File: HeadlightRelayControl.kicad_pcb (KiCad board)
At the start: 2 copper layers, 49.5 x 49.5 mm, 30 parts, among them P1 CONN_01X03, P2 CONN_01X02, P3 CONN_01X02, P4 CONN_2, Q1 2N3904, Q2 2N3904

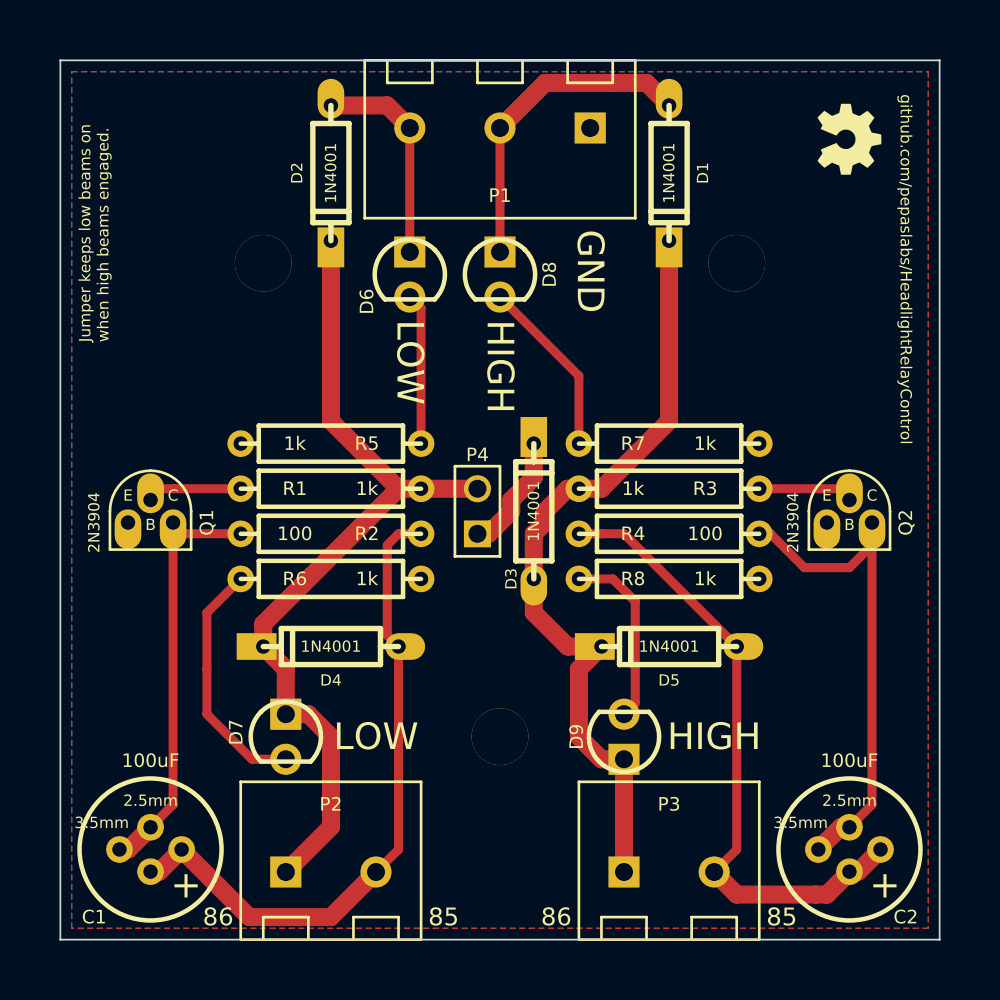
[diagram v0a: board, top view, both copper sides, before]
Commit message: bugfix: a 1/4 watt resistor was seeing 500mW.  broke it up into four 1/4w resistors.  this is release v2.
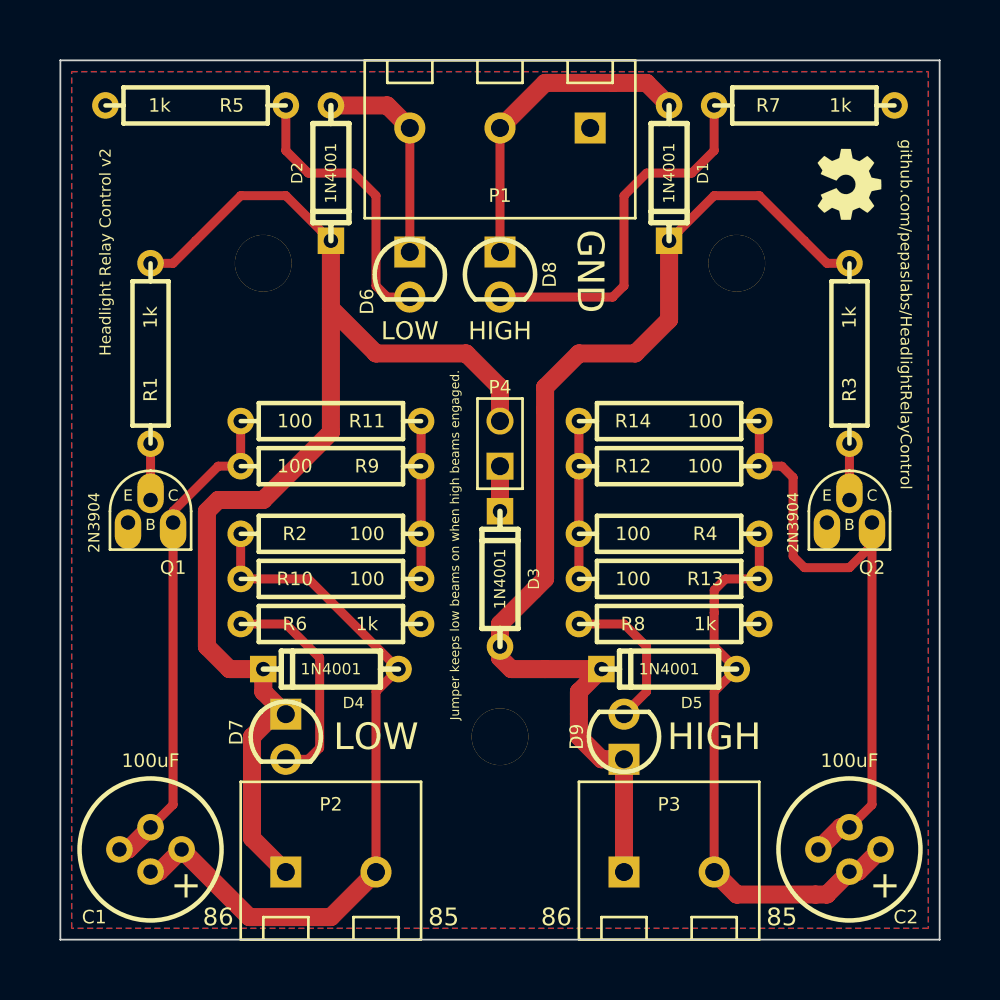
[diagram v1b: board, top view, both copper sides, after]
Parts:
- added R10: 100, R_AXIAL_0W25_059A, F.Cu at (94.0, 95.2)
- added R11: 100, R_AXIAL_0W25_059A, F.Cu at (104.1, 86.4)
- added R12: 100, R_AXIAL_0W25_059A, F.Cu at (113.0, 88.9)
- added R13: 100, R_AXIAL_0W25_059A, F.Cu at (123.2, 95.2)
- added R14: 100, R_AXIAL_0W25_059A, F.Cu at (113.0, 86.4)
- added R9: 100, R_AXIAL_0W25_059A, F.Cu at (104.1, 88.9)
- D1, D2, D3, D4, D5: footprint DIODE_3 -> DIODE_3_059A
- moved R5 20.5 mm to (96.5, 68.6)
- moved R7 20.5 mm to (120.7, 68.6)
- moved R2 10.2 mm to (94.0, 92.7), turned to 0 degrees
- moved R4 10.2 mm to (123.2, 92.7), turned to 180 degrees
- moved R3 5.68 mm to (128.3, 87.6), turned to 90 degrees
- moved R1 5.68 mm to (88.9, 87.6), turned to 90 degrees
- moved D3 4.26 mm to (108.6, 99.1)
- moved P4 4.02 mm to (108.6, 87.6)
- moved G*** 2.54 mm to (128.3, 73.0)
- moved R6 2.54 mm to (94.0, 97.8)
- moved R8 2.54 mm to (113.0, 97.8)
- moved D4 1.27 mm to (102.9, 100.3)
- moved D5 1.27 mm to (121.9, 100.3)
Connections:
- C1 pad 2: N-0000020 -> N-0000022
- C2 pad 2: N-0000010 (its old number) -> N-0000013
- Q1 pad 3: N-0000020 -> N-0000022
- Q2 pad 3: N-0000010 (its old number) -> N-0000013
- R2 pad 2: N-0000020 -> N-0000015
- R4 pad 2: N-0000010 (its old number) -> N-0000014
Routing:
- net N-0000013: track 0.00 -> 35.6 mm
- net N-0000010 (its old number): track 28.9 -> 0.00 mm
- net N-0000022: track 0.00 -> 28.0 mm
- net N-0000020: track 24.0 -> 0.00 mm
- net LowBeamControl: track 48.1 -> 70.9 mm
- net HighBeamControl: track 44.8 -> 61.8 mm
- net N-000004: track 10.1 -> 21.0 mm
- net N-0000015: track 0.00 -> 8.89 mm
- net N-0000014: track 0.00 -> 8.89 mm
- net N-000003: track 8.52 -> 15.9 mm
- net N-0000016: track 6.77 -> 2.54 mm
- net N-0000017: track 37.2 -> 41.3 mm
- net N-0000024: track 35.7 -> 33.2 mm
- net N-0000018: track 5.34 -> 3.18 mm
- net N-0000023: track 5.34 -> 3.18 mm
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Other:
- board text added: "Headlight Relay Control v2"

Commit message: removing extraneous transistors. updated board labelling.
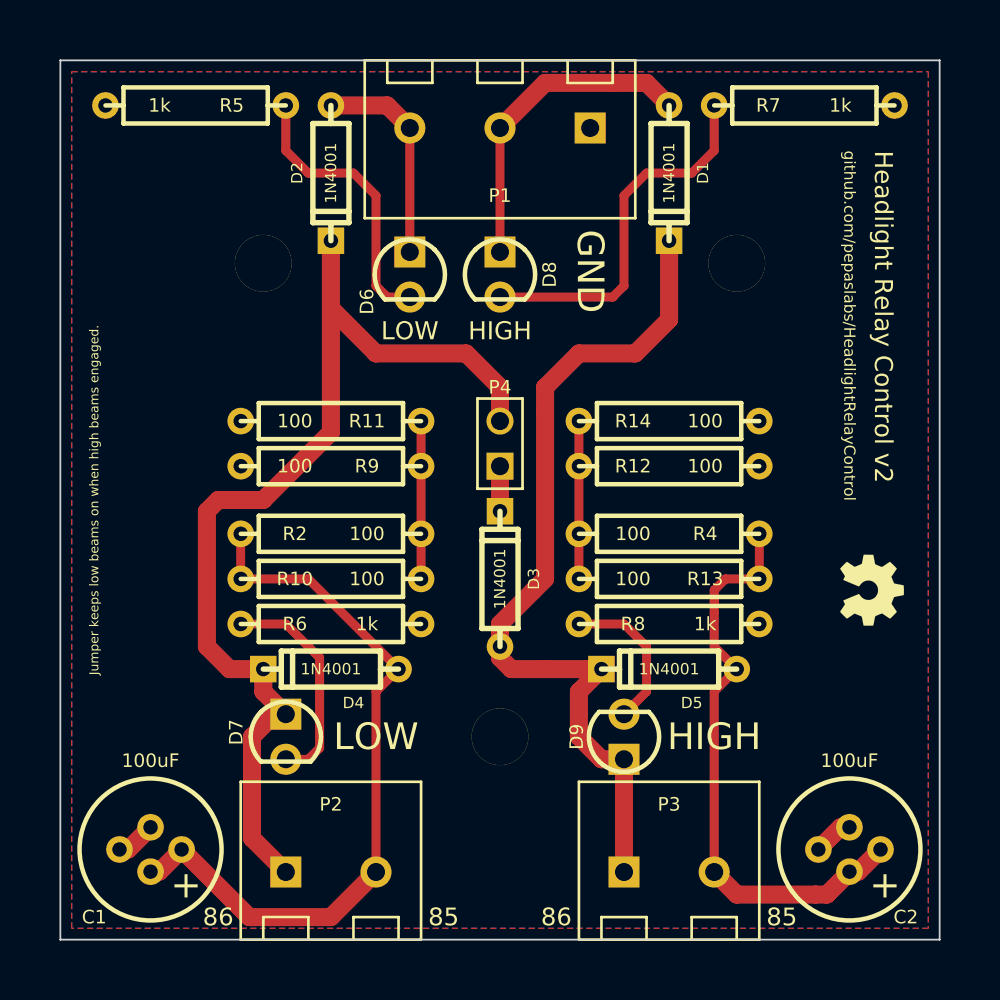
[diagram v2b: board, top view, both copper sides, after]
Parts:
- removed Q1, Q2: 2N3904, TO-92_Q_EBC
- removed R1, R3: 1k, R_AXIAL_0W25_059A
- moved G*** 22.9 mm to (129.5, 95.9)
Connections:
- C1 pad 2: N-0000022 -> GND
- C2 pad 2: N-0000013 (its old number) -> GND
- R11 pad 2: N-0000022 -> GND
- R12 pad 2: N-0000013 (its old number) -> GND
- R14 pad 2: N-0000013 (its old number) -> GND
- R9 pad 2: N-0000022 -> GND
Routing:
- net N-0000013 (its old number): track 35.6 -> 0.00 mm
- net N-0000022: track 28.0 -> 0.00 mm
- net HighBeamControl: track 61.8 -> 49.0 mm
- net LowBeamControl: track 70.9 -> 58.1 mm
- net GND: track 0.00 -> 4.54 mm
- net N-0000023: track 3.18 -> 0.00 mm
- net N-0000018 (its old number): track 3.18 -> 0.00 mm
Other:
- board text added: "+"
- board text added: "-"

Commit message: Added corner mounting holes.
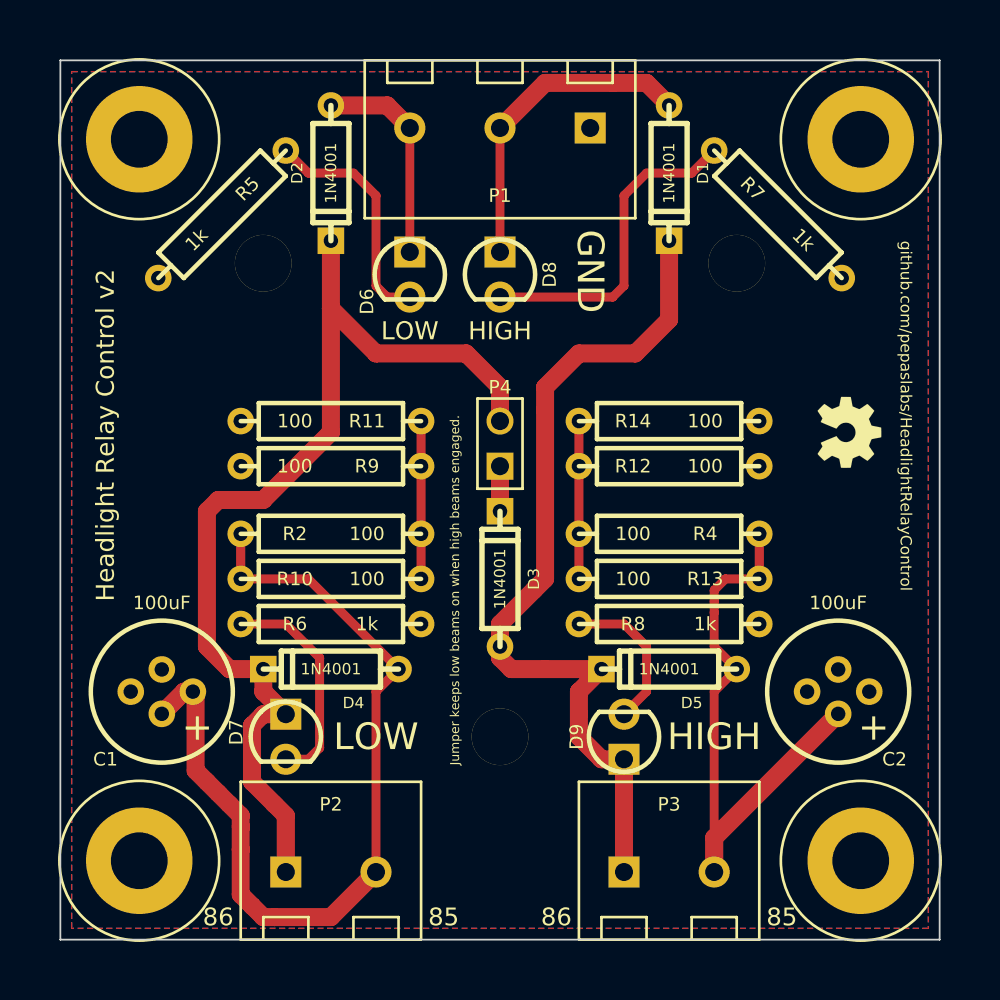
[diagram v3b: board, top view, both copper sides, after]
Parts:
- added H10: HOLE, hole_M3, F.Cu at (88.3, 111.1)
- added H4: HOLE, hole_M3, F.Cu at (88.3, 70.5)
- added H8: HOLE, hole_M3, F.Cu at (128.9, 70.5)
- added H9: HOLE, hole_M3, F.Cu at (128.9, 111.1)
- moved G*** 8.98 mm to (128.3, 87.0)
- moved C1 8.91 mm to (89.5, 101.6)
- moved C2 8.91 mm to (127.6, 101.6)
- moved R5 2.54 mm to (96.5, 71.1), turned to 225 degrees
- moved R7 2.54 mm to (120.7, 71.1), turned to 315 degrees
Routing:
- net N-0000017: track 41.3 -> 49.5 mm
- net GND: track 4.54 -> 0.00 mm
- net N-000009: track 15.9 -> 13.4 mm
- net N-000003: track 21.0 -> 18.5 mm
- net N-0000024: track 33.2 -> 34.1 mm

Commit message: adding v3 board design with constant current sinks on relay coils.
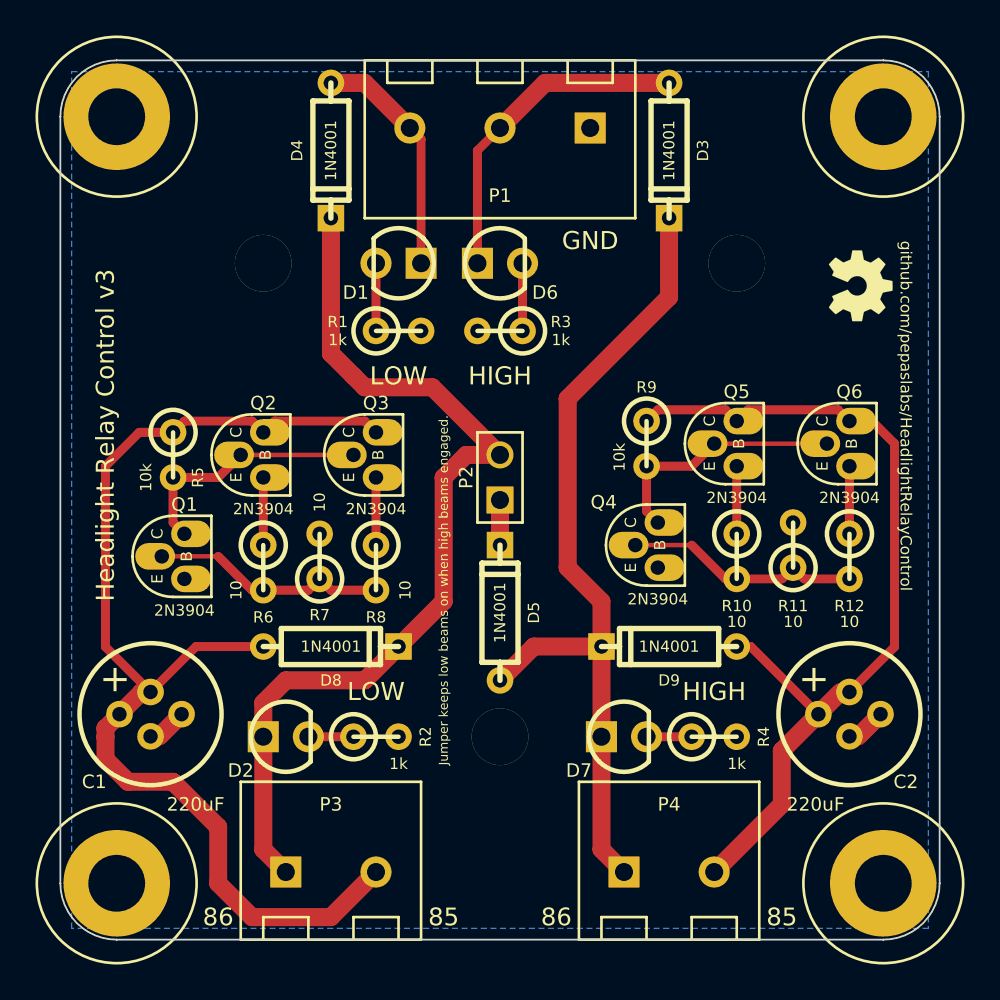
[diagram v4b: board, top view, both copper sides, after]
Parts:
- removed H4: HOLE, hole_M3
- removed R13, R14: 100, R_AXIAL_0W25_059A
- added H7: HOLE, hole_M3, F.Cu at (130.2, 112.4)
- added Q1: 2N3904, TO-92_Q_EBC, F.Cu at (90.8, 95.2)
- added Q2: 2N3904, TO-92_Q_EBC, F.Cu at (95.2, 89.5)
- added Q3: 2N3904, TO-92_Q_EBC, F.Cu at (101.6, 89.5)
- added Q4: 2N3904, TO-92_Q_EBC, F.Cu at (117.5, 94.6)
- added Q5: 2N3904, TO-92_Q_EBC, F.Cu at (121.9, 88.9)
- added Q6: 2N3904, TO-92_Q_EBC, F.Cu at (128.3, 88.9)
- added R1: 1k, R_AXIAL_0W25_V_059A, F.Cu at (101.6, 81.3)
- added R3: 1k, R_AXIAL_0W25_V_059A, F.Cu at (109.9, 81.3)
- C1, C2: value 100uF -> 220uF
- D1, D2: value 1N4001 -> LED; footprint DIODE_3_059A -> LED_3MM_069A
- D8, D9: value LED -> 1N4001; footprint LED_3MM_069A -> DIODE_3_059A
- P2: value CONN_01X02 -> CONN_2; footprint TERMINAL_BLOCK_2_5mm -> PIN_ARRAY_2X1
- P4: value CONN_2 -> CONN_01X02; footprint PIN_ARRAY_2X1 -> TERMINAL_BLOCK_2_5mm
- R10, R11, R12: value 100 -> 10; footprint R_AXIAL_0W25_059A -> R_AXIAL_0W25_V_059A
- R2, R4: value 100 -> 1k; footprint R_AXIAL_0W25_059A -> R_AXIAL_0W25_V_059A
- R5: value 1k -> 10k; footprint R_AXIAL_0W25_059A -> R_AXIAL_0W25_V_059A
- R6, R7, R8: value 1k -> 10; footprint R_AXIAL_0W25_059A -> R_AXIAL_0W25_V_059A
- R9: value 100 -> 10k; footprint R_AXIAL_0W25_059A -> R_AXIAL_0W25_V_059A
- moved H8 59.3 mm to (87.0, 112.4)
- moved H10 41.9 mm to (87.0, 69.2)
- moved H9 41.9 mm to (130.2, 69.2)
- moved D2 35.8 mm to (95.2, 104.1), turned to 0 degrees
- moved D4 33.2 mm to (99.1, 67.3), turned to 270 degrees
- moved D3 33.1 mm to (118.1, 67.3), turned to 270 degrees
- moved R7 32.8 mm to (98.4, 95.2), turned to 90 degrees
- moved R10 28.1 mm to (121.9, 92.7), turned to 270 degrees
- moved H2 26.7 mm to (95.2, 77.5)
- moved H3 26.7 mm to (121.9, 77.5)
- moved P4 25.9 mm to (118.1, 111.8), turned to 0 degrees
- moved D8 25.9 mm to (95.2, 99.1), turned to 0 degrees
- moved P2 24.2 mm to (108.6, 89.5), turned to 90 degrees
- moved R11 22.5 mm to (125.1, 94.6), turned to 90 degrees
- moved P3 19.0 mm to (99.1, 111.8)
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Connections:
- C1 pad 1: N-0000017 -> N-000007
- C2 pad 1: N-0000024 -> N-000002
- D1 pad 1: HighBeamSignal -> LowBeamSignal
- D1 pad 2: HighBeamControl -> N-0000015
- D2 pad 1: LowBeamSignal -> LowBeamControl
- D2 pad 2: LowBeamControl -> N-0000030
- D3 pad 1: HighBeamControl -> HighBeamSignal
- D3 pad 2: N-0000022 -> HighBeamControl
- D4 pad 1: N-0000017 -> LowBeamSignal
- D5 pad 1: N-0000024 -> HighBeamControl
- D5 pad 2: HighBeamControl -> N-0000028
- D6 pad 1: LowBeamSignal -> HighBeamSignal
- D6 pad 2: N-000009 -> N-0000016
- D7 pad 1: LowBeamControl -> HighBeamControl
- D7 pad 2: N-0000023 -> N-0000014
- D8 pad 1: HighBeamSignal -> N-000007
- D8 pad 2: N-000003 -> LowBeamControl
- D9 pad 1: HighBeamControl -> N-000002
- D9 pad 2: N-000008 -> HighBeamControl
- P2 pad 1: LowBeamControl -> N-0000028
- P2 pad 2: N-0000017 -> LowBeamControl
- P3 pad 1: HighBeamControl -> LowBeamControl
- P3 pad 2: N-0000024 -> N-000007
- P4 pad 1: N-0000022 -> HighBeamControl
- P4 pad 2: LowBeamControl -> N-000002
- R10 pad 1: N-0000017 -> N-000005
- R10 pad 2: N-0000011 -> N-000004
- R11 pad 1: N-0000011 -> N-000004
- R12 pad 1: N-0000016 -> N-000006
- R12 pad 2: GND -> N-000004
- R2 pad 1: N-0000017 -> N-0000030
- R2 pad 2: N-0000011 -> GND
- R4 pad 1: N-0000024 -> N-0000014
- R4 pad 2: N-0000016 -> GND
- R5 pad 1: N-000009 -> N-000007
- R5 pad 2: GND -> N-000001
- R6 pad 1: N-0000023 -> N-000009
- R6 pad 2: GND -> N-0000010
- R7 pad 1: N-000003 -> N-0000010
- R8 pad 2: GND -> N-0000010
- R9 pad 1: N-0000011 -> N-000002
- R9 pad 2: GND -> N-0000012
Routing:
- net N-000007: track 0.00 -> 65.2 mm
- net N-000002: track 0.00 -> 50.4 mm
- net N-0000017: track 49.5 -> 0.00 mm
- net N-0000024: track 34.1 -> 0.00 mm
- net N-000003: track 18.5 -> 0.00 mm
- net N-000001: track 0.00 -> 14.1 mm
- net N-0000012: track 0.00 -> 14.1 mm
- net N-000004: track 0.00 -> 13.4 mm
- net N-0000010: track 0.00 -> 13.4 mm
- net N-0000023: track 12.5 -> 0.00 mm
- net N-000009: track 13.4 -> 3.81 mm
- net N-0000011: track 8.89 -> 0.00 mm
- net LowBeamControl: track 58.5 -> 52.8 mm
- net N-0000016: track 8.89 -> 3.81 mm
- net N-000008: track 8.67 -> 3.81 mm
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- removed copper zone on F.Cu, net (none)
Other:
- outline, holes or cut-outs redrawn
- board text added: "Headlight Relay Control v3"
- board text removed: "Headlight Relay Control v2"
